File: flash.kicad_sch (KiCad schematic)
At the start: 0 parts

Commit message: [#103224] Add QSPI Flash section, add .ci.yml
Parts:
- added C5001: C_100n_0402, antmicro-footprints:C_0402_1005Metric, symbol antmicroCapacitors0402:C_100n_0402
- added C5002: C_100n_0402, antmicro-footprints:C_0402_1005Metric, symbol Capacitors0402:C_100n_0402
- added J5001: PinHeader_1x2_P2.54mm_Drill1.02mm, antmicro-footprints:PinHeader_1x2_P2.54mm_Drill1.02mm, symbol GenericPinHeaders:PinHeader_1x2_P2.54mm_Drill1.02mm
- added J5002: Socket_SOP2-16_ACA-SPI-006-K01_Flash_CUSTOM, antmicro-footprints:Socket_SOP2-16_ACA-SPI-006-K01, symbol MechanicalParts:Socket_SOP2-16_ACA-SPI-006-K01_Flash_CUSTOM
- added J5003: PinHeader_2x4_P2.54mm_Drill1.02mm, antmicro-footprints:PinHeader_2x4_P2.54mm_Drill1.02mm, symbol Antmicro Symbols:PinHeader_2x4_P2.54mm_Drill1.02mm
- added R5001, R5002, R5003, R5004, R5005, R5006, R5008: R_10k_0402, antmicro-footprints:R_0402_1005Metric, symbol antmicroResistors0402:R_10k_0402
- added R5007: R_1k_0402, antmicro-footprints:R_0402_1005Metric, symbol Antmicro Symbols:R_1k_0402
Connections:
- new net: J5001.1, R5007.1
- new net: J5002.3 (~{RESET}), R5008.1
- new net +1V8: C5001.2, C5002.2, J5002.14 (VIO), J5002.2 (VCC), J5003.1, R5001.2, R5002.2, R5003.2, R5004.2, R5005.2, R5006.2, R5008.2
- new net EC_QSPI.IO0: J5002.15 (SI/IO0), J5003.6, R5003.1
- new net EC_QSPI.IO1: J5002.8 (SO/IO1), J5003.5, R5004.1
- new net EC_QSPI.IO2: J5002.9 (~{WP/IO2}), J5003.7, R5005.1
- new net EC_QSPI.IO3: J5002.1 (~{HOLD/IO3}), J5003.8, R5006.1
- new net EC_QSPI.SCK: J5002.16 (SCK), J5003.4, R5001.1
- new net EC_QSPI.~{CS0}: J5002.7 (~{CS}), J5003.3, R5002.1, R5007.2
- new net GND: C5001.1, C5002.1, J5001.2, J5002.10 (VSS), J5003.2
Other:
- note added: "BSS_STRAP"
- note added: "From Eval: GigaDevice GD25LR256EFIR"
- note added: "QSPI Flash"

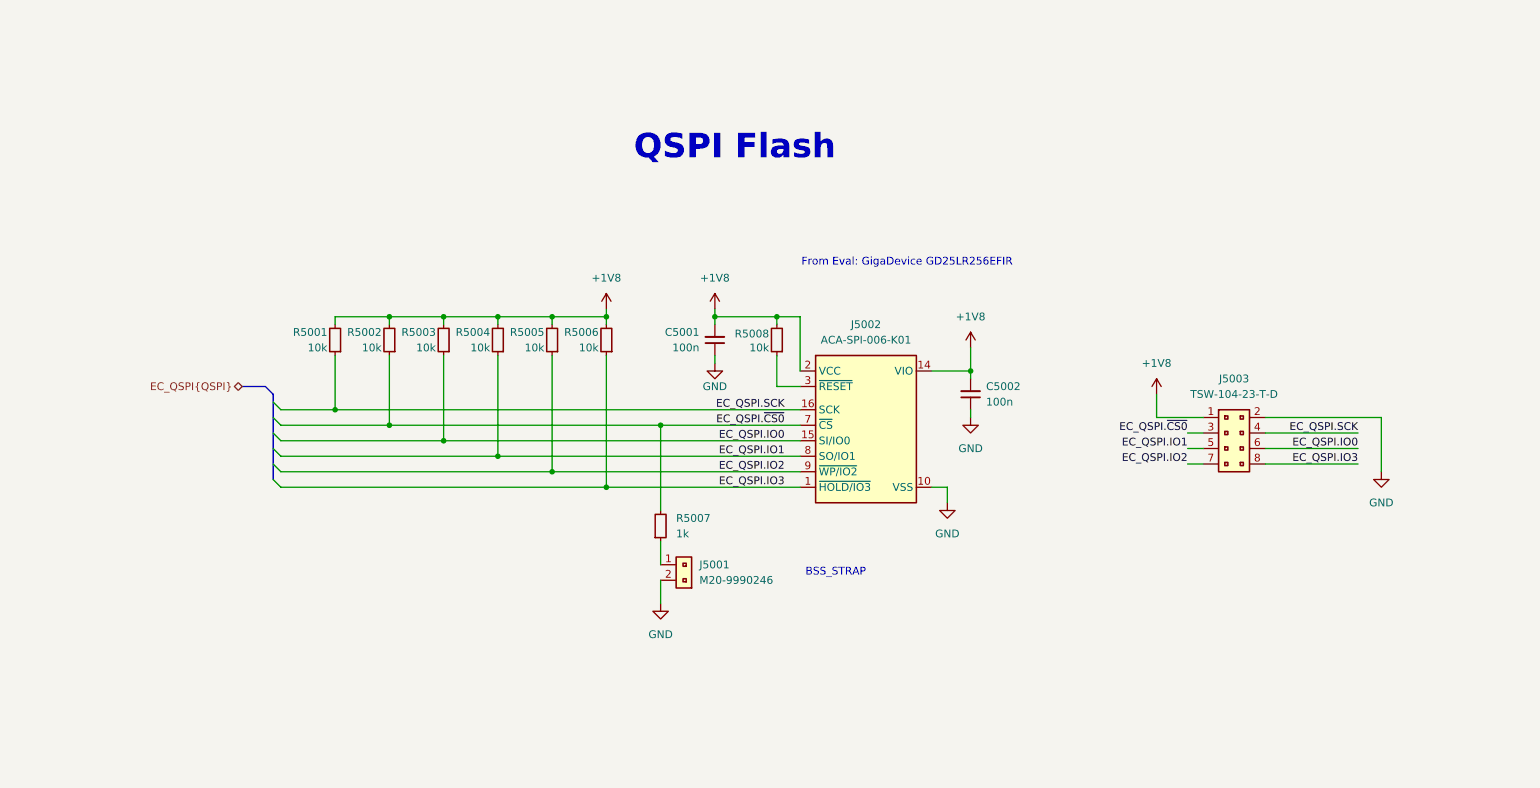
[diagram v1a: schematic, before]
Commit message: [#103224] Add JTAG connector, add 2nd QSPI flash in co-layout, add Antmicro and OSH logos
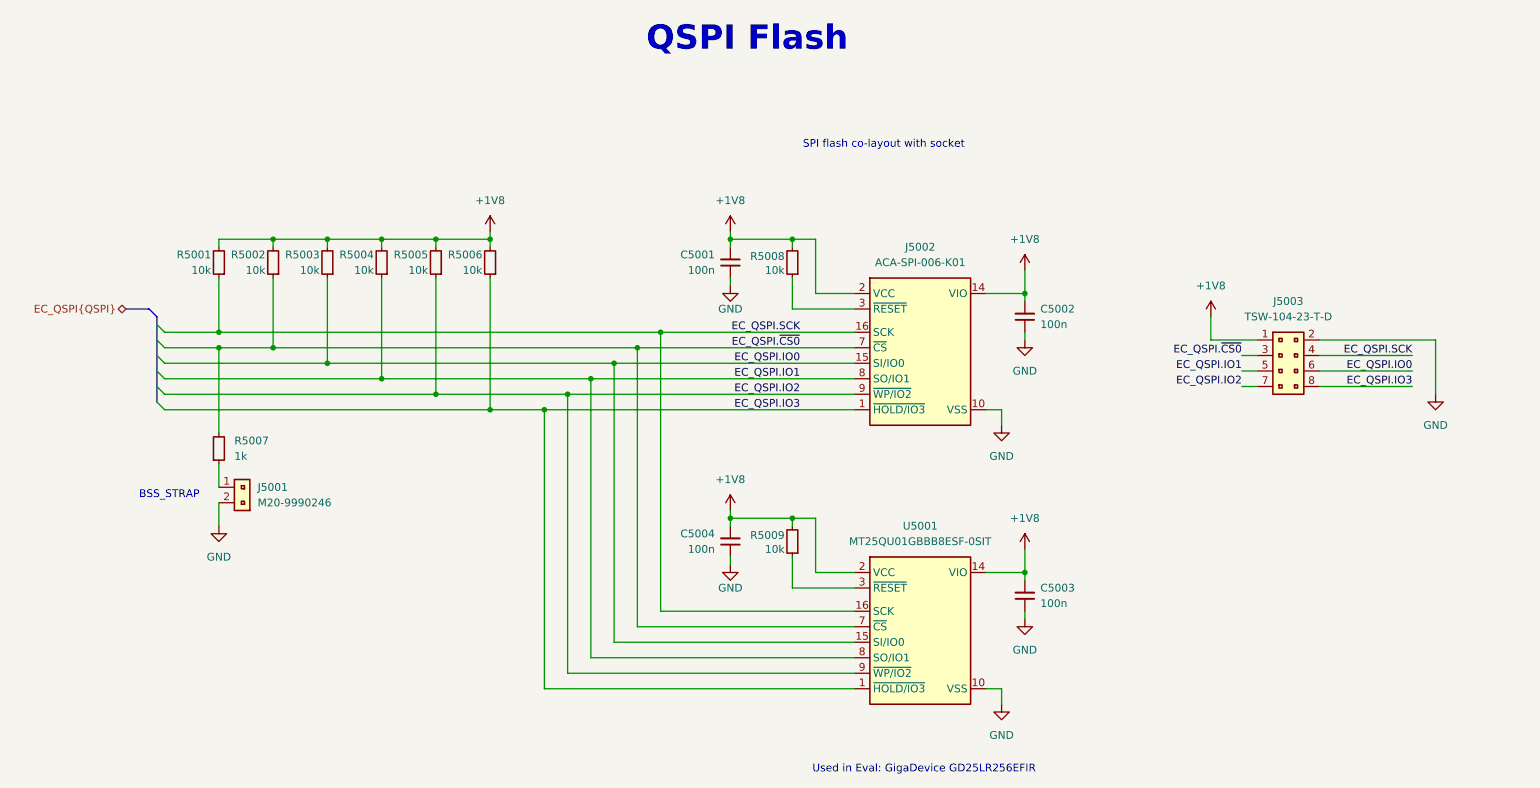
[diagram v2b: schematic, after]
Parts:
- added C5003: C_100n_0402, antmicro-footprints:C_0402_1005Metric, symbol Capacitors0402:C_100n_0402
- added C5004: C_100n_0402, antmicro-footprints:C_0402_1005Metric, symbol antmicroCapacitors0402:C_100n_0402
- added R5009: R_10k_0402, antmicro-footprints:R_0402_1005Metric, symbol antmicroResistors0402:R_10k_0402
- added U5001: MT25QU01GBBB8_SOIC, antmicro-footprints:SOIC-16_W7.5mm, symbol Antmicro Symbols:MT25QU01GBBB8_SOIC
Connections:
- net +1V8: now also C5003.2, C5004.2, R5009.2, U5001.14 (VIO), U5001.2 (VCC)
- net EC_QSPI.IO0: now also U5001.15 (SI/IO0)
- net EC_QSPI.IO1: now also U5001.8 (SO/IO1)
- net EC_QSPI.IO2: now also U5001.9 (~{WP/IO2})
- net EC_QSPI.IO3: now also U5001.1 (~{HOLD/IO3})
- net EC_QSPI.SCK: now also U5001.16 (SCK)
- net EC_QSPI.~{CS0}: now also U5001.7 (~{CS})
- net GND: now also C5003.1, C5004.1, U5001.10 (VSS)
- new net: U5001.11 (DNU), U5001.12 (DNU), U5001.4 (DNU), U5001.5 (DNU)
- new net: R5009.1, U5001.3 (~{RESET})
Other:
- note added: "SPI flash co-layout with socket"
- note added: "Used in Eval: GigaDevice GD25LR256EFIR"
- note removed: "From Eval: GigaDevice GD25LR256EFIR"
- moved on the sheet: C5001, C5002, J5001, J5002, J5003, R5001, R5002, R5003, R5004, R5005, R5006, R5007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

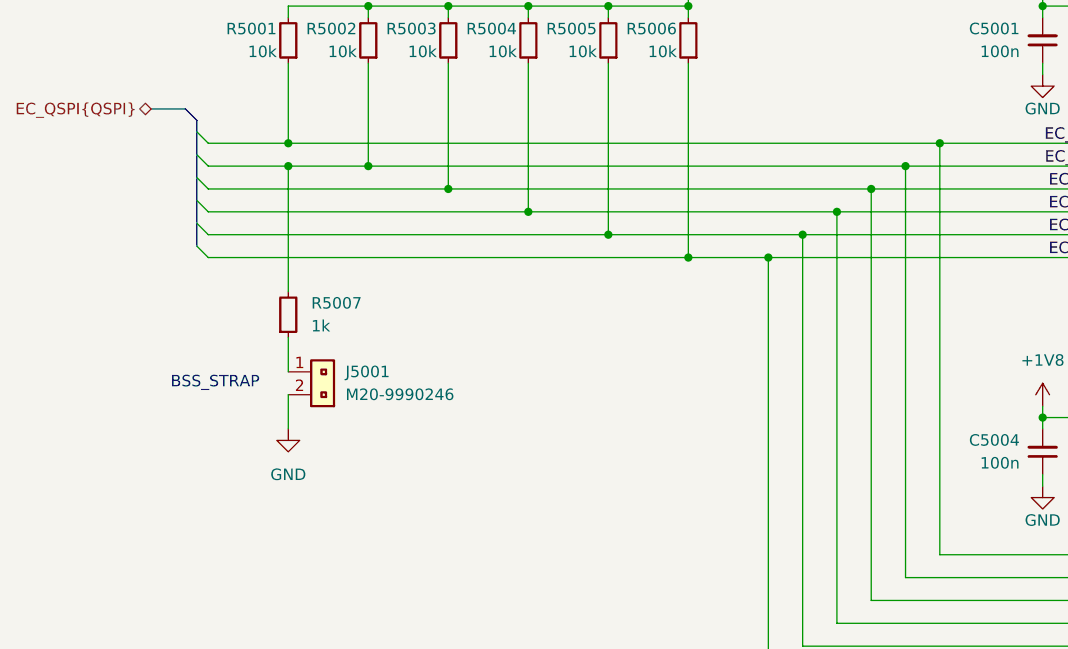
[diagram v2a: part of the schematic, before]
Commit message: [#103224] Change buffer ICs, change JTAG connector, move BSS_STRAP resistors to MEC1723 sheet
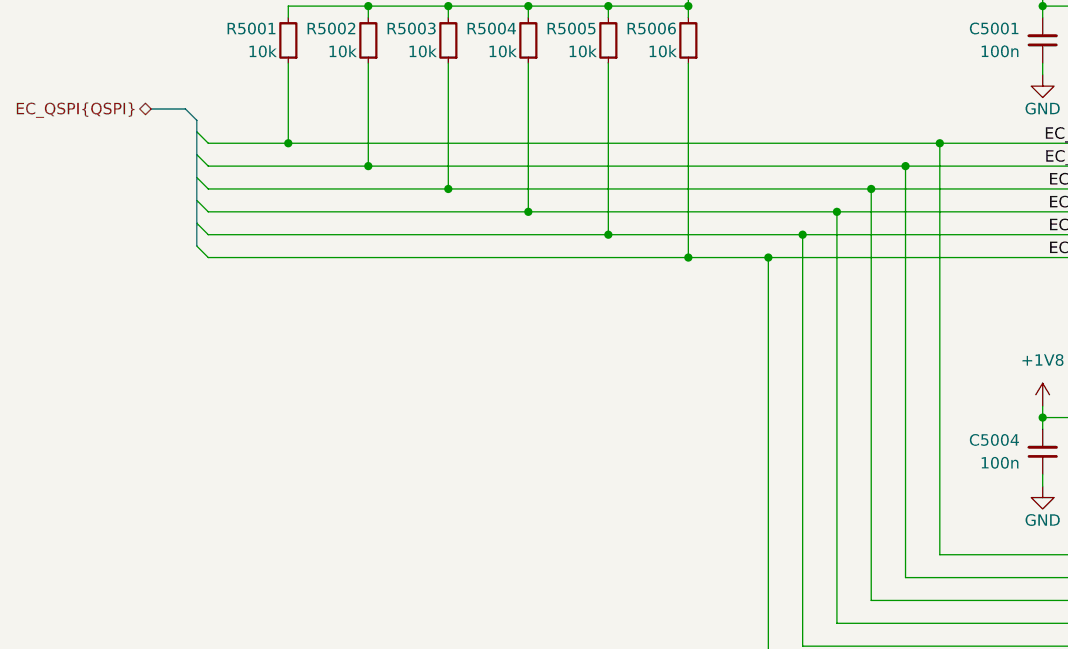
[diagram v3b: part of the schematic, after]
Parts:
- removed J5001: PinHeader_1x2_P2.54mm_Drill1.02mm, antmicro-footprints:PinHeader_1x2_P2.54mm_Drill1.02mm, symbol GenericPinHeaders:PinHeader_1x2_P2.54mm_Drill1.02mm
- removed R5007: R_1k_0402, antmicro-footprints:R_0402_1005Metric, symbol Antmicro Symbols:R_1k_0402
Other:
- note removed: "BSS_STRAP"

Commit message: [#103224] Route 7segment buffers, fix minor typos,add TODO list
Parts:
- added J5001: Tag-Connect_TC2050-IDC-NL_2x5_P1.27mm, antmicro-footprints:Tag-Connect_TC2050-IDC-NL_2x5_P1.27mm, symbol Antmicro Symbols:Tag-Connect_TC2050-IDC-NL_2x5_P1.27mm
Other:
- moved on the sheet: J5003
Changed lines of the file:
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@@
 	(wire
 		(pts
-			(xy 231.14 85.09) (xy 223.52 85.09)
+			(xy 238.76 67.31) (xy 231.14 67.31)
 		)
 		(stroke
@@
 	(wire
 		(pts
-			(xy 260.35 85.09) (xy 260.35 93.98)
+			(xy 267.97 67.31) (xy 267.97 76.2)
 		)
 		(stroke
@@
 	(wire
 		(pts
-			(xy 228.6 87.63) (xy 231.14 87.63)
+			(xy 236.22 69.85) (xy 238.76 69.85)
 		)
 		(stroke
@@
 	(wire
 		(pts
-			(xy 223.52 85.09) (xy 223.52 81.28)
+			(xy 231.14 67.31) (xy 231.14 63.5)
 		)
 		(stroke
@@
 	(wire
 		(pts
-			(xy 256.54 87.63) (xy 241.3 87.63)
+			(xy 264.16 69.85) (xy 248.92 69.85)
 		)
 		(stroke
@@
 	(wire
 		(pts
-			(xy 241.3 85.09) (xy 260.35 85.09)
+			(xy 248.92 67.31) (xy 267.97 67.31)
 		)
 		(stroke
@@
 	(wire
 		(pts
-			(xy 256.54 92.71) (xy 241.3 92.71)
+			(xy 264.16 74.93) (xy 248.92 74.93)
 		)
 		(stroke
@@
 	(wire
 		(pts
-			(xy 256.54 90.17) (xy 241.3 90.17)
+			(xy 264.16 72.39) (xy 248.92 72.39)
 		)
 		(stroke
@@
 	(wire
 		(pts
-			(xy 228.6 90.17) (xy 231.14 90.17)
+			(xy 236.22 72.39) (xy 238.76 72.39)
 		)
 		(stroke
@@
 	(wire
 		(pts
-			(xy 228.6 92.71) (xy 231.14 92.71)
+			(xy 236.22 74.93) (xy 238.76 74.93)
 		)
 		(stroke
@@
 	)
 	(label "EC_QSPI.IO0"
-		(at 256.54 90.17 180)
+		(at 264.16 72.39 180)
 		(effects
 			(font
@@
 	)
 	(label "EC_QSPI.~{CS0}"
-		(at 228.6 87.63 180)
+		(at 236.22 69.85 180)
 		(effects
 			(font
@@
 	)
 	(label "EC_QSPI.IO2"
-		(at 228.6 92.71 180)
+		(at 236.22 74.93 180)
 		(effects
 			(font
@@
 	)
 	(label "EC_QSPI.IO1"
-		(at 228.6 90.17 180)
+		(at 236.22 72.39 180)
 		(effects
 			(font
@@
 	)
 	(label "EC_QSPI.SCK"
-		(at 256.54 87.63 180)
+		(at 264.16 69.85 180)
 		(effects
 			(font
@@
 	)
 	(label "EC_QSPI.IO3"
-		(at 256.54 92.71 180)
+		(at 264.16 74.93 180)
 		(effects
 			(font
@@
 	(symbol
 		(lib_id "Antmicro Symbols:GND")
-		(at 260.35 93.98 0)
+		(at 267.97 76.2 0)
 		(unit 1)
 		(body_style 1)
@@
 		(fields_autoplaced yes)
 		(property "Reference" "#PWR05009"
-			(at 269.24 96.52 0)
+			(at 276.86 78.74 0)
 			(hide yes)
 			(show_name no)
@@
 		)
 		(property "Value" "GND"
-			(at 260.35 99.06 0)
+			(at 267.97 81.28 0)
 			(show_name no)
 			(do_not_autoplace no)
@@
 		)
 		(property "Footprint" ""
-			(at 269.24 101.6 0)
+			(at 276.86 83.82 0)
 			(hide yes)
 			(show_name no)
@@
 		)
 		(property "Datasheet" ""
-			(at 269.24 106.68 0)
+			(at 276.86 88.9 0)
 			(hide yes)
 			(show_name no)
@@
 		)
 		(property "Description" ""
-			(at 269.24 109.22 0)
+			(at 276.86 91.44 0)
 			(hide yes)
 			(show_name no)
@@
 		)
 		(property "Author" "Antmicro"
-			(at 269.24 101.6 0)
+			(at 276.86 83.82 0)
 			(hide yes)
 			(show_name no)
@@
 		)
 		(property "License" "Apache-2.0"
-			(at 269.24 104.14 0)
+			(at 276.86 86.36 0)
 			(hide yes)
 			(show_name no)
@@
 	(symbol
 		(lib_id "antmicropower:+1V8")
-		(at 223.52 81.28 0)
+		(at 231.14 63.5 0)
 		(unit 1)
 		(body_style 1)
@@
 		(fields_autoplaced yes)
 		(property "Reference" "#PWR05008"
-			(at 238.76 83.82 0)
+			(at 246.38 66.04 0)
 			(hide yes)
 			(show_name no)
@@
 		)
 		(property "Value" "+1V8"
-			(at 223.52 76.2 0)
+			(at 231.14 58.42 0)
 			(show_name no)
 			(do_not_autoplace no)
@@
 		)
 		(property "Footprint" ""
-			(at 238.76 88.9 0)
+			(at 246.38 71.12 0)
 			(hide yes)
 			(show_name no)
@@
 		)
 		(property "Datasheet" ""
-			(at 238.76 91.44 0)
+			(at 246.38 73.66 0)
 			(hide yes)
 			(show_name no)
@@
 		)
 		(property "Description" ""
-			(at 238.76 93.98 0)
+			(at 246.38 76.2 0)
 			(hide yes)
 			(show_name no)
@@
 		)
 		(property "Author" "Antmicro"
-			(at 238.76 86.36 0)
+			(at 246.38 68.58 0)
 			(hide yes)
 			(show_name no)
@@
 		)
 		(property "License" "Apache-2.0"
-			(at 238.76 88.9 0)
+			(at 246.38 71.12 0)
 			(hide yes)
 			(show_name no)
@@
 	(symbol
 		(lib_id "Antmicro Symbols:PinHeader_2x4_P2.54mm_Drill1.02mm")
-		(at 231.14 85.09 0)
+		(at 238.76 67.31 0)
 		(unit 1)
 		(body_style 1)
@@
 		(fields_autoplaced yes)
 		(property "Reference" "J5003"
-			(at 236.22 78.74 0)
+			(at 243.84 60.96 0)
 			(show_name no)
 			(do_not_autoplace no)
@@
 		)
 		(property "Value" "PinHeader_2x4_P2.54mm_Drill1.02mm"
-			(at 256.54 90.17 0)
+			(at 264.16 72.39 0)
 			(hide yes)
 			(show_name no)
@@
 		)
 		(property "Footprint" "antmicro-footprints:PinHeader_2x4_P2.54mm_Drill1.02mm"
-			(at 256.54 92.71 0)
+			(at 264.16 74.93 0)
 			(hide yes)
 			(show_name no)
@@
 		)
 		(property "Datasheet" "https://suddendocs.samtec.com/catalog_english/tsw_th.pdf"
-			(at 256.54 95.25 0)
+			(at 264.16 77.47 0)
 			(hide yes)
 			(show_name no)
@@
 		)
 		(property "Description" "Header 2.54mm pitch THT 8P in Dual Pin Header"
-			(at 256.54 107.95 0)
+			(at 264.16 90.17 0)
 			(hide yes)
 			(show_name no)
@@
 		)
 		(property "MPN" "TSW-104-23-T-D"
-			(at 236.22 81.28 0)
+			(at 243.84 63.5 0)
 			(show_name no)
 			(do_not_autoplace no)
@@
 		)
 		(property "Manufacturer" "Samtec"
-			(at 256.54 100.33 0)
+			(at 264.16 82.55 0)
 			(hide yes)
 			(show_name no)
@@
 		)
 		(property "Author" "Antmicro"
-			(at 256.54 102.87 0)
+			(at 264.16 85.09 0)
 			(hide yes)
 			(show_name no)
@@
 		)
 		(property "License" "Apache-2.0"
-			(at 256.54 105.41 0)
+			(at 264.16 87.63 0)
 			(hide yes)
 			(show_name no)
@@
 					(unit 1)
 				)
+			)
+		)
+	)
+	(symbol
+		(lib_id "Antmicro Symbols:Tag-Connect_TC2050-IDC-NL_2x5_P1.27mm")
+		(at 228.6 97.79 0)
+		(unit 1)
+		(body_style 1)
+		(exclude_from_sim no)
+		(in_bom no)
+		(on_board yes)
+		(in_pos_files yes)
+		(dnp no)
+		(fields_autoplaced yes)
+		(property "Reference" "J5001"
+			(at 244.475 90.17 0)
+			(show_name no)
+			(do_not_autoplace no)
+			(effects
+				(font
+					(size 1.27 1.27)
+					(thickness 0.15)
+				)
+			)
+		)
+		(property "Value" "Tag-Connect_TC2050-IDC-NL_2x5_P1.27mm"
+			(at 267.97 101.6 0)
+			(hide yes)
+			(show_name no)
+			(do_not_autoplace no)
+			(effects
+				(font
+					(size 1.27 1.27)
+					(thickness 0.15)
+				)
+				(justify left bottom)
+			)
+		)
+		(property "Footprint" "antmicro-footprints:Tag-Connect_TC2050-IDC-NL_2x5_P1.27mm"
+			(at 267.97 104.14 0)
+			(hide yes)
+			(show_name no)
+			(do_not_autoplace no)
+			(effects
+				(font
+					(size 1.27 1.27)
+					(thickness 0.15)
+				)
+				(justify left bottom)
+			)
+		)
+		(property "Datasheet" "https://www.tag-connect.com/wp-content/uploads/bsk-pdf-manager/TC2050-IDC-NL_Datasheet_8.pdf"
+			(at 267.97 106.68 0)
+			(hide yes)
+			(show_name no)
+			(do_not_autoplace no)
+			(effects
+				(font
+					(size 1.27 1.27)
+					(thickness 0.15)
+				)
+				(justify left bottom)
+			)
+		)
+		(property "Description" "Tag Connect 2x5 1.27mm terminal"
+			(at 267.97 119.38 0)
+			(hide yes)
+			(show_name no)
+			(do_not_autoplace no)
+			(effects
+				(font
+					(size 1.27 1.27)
+				)
+				(justify left bottom)
+			)
+		)
+		(property "MPN" "TC2050-IDC-NL"
+			(at 244.475 92.71 0)
+			(show_name no)
+			(do_not_autoplace no)
+			(effects
+				(font
+					(size 1.27 1.27)
+					(thickness 0.15)
+				)
+			)
+		)
+		(property "Manufacturer" "Tag Connect"
+			(at 267.97 111.76 0)
+			(hide yes)
+			(show_name no)
+			(do_not_autoplace no)
+			(effects
+				(font
+					(size 1.27 1.27)
+					(thickness 0.15)
+				)
+				(justify left bottom)
+			)
+		)
+		(property "Author" "Antmicro"
+			(at 267.97 114.3 0)
+			(hide yes)
+			(show_name no)
+			(do_not_autoplace no)
+			(effects
+				(font
+					(size 1.27 1.27)
+					(thickness 0.15)
+				)
+				(justify left bottom)
+			)
+		)
+		(property "License" "Apache-2.0"
+			(at 267.97 116.84 0)
+			(hide yes)
+			(show_name no)
+			(do_not_autoplace no)
+			(effects
+				(font
+					(size 1.27 1.27)
+					(thickness 0.15)
+				)
+				(justify left bottom)
+			)
+		)
+		(pin "2"
+		)
+		(pin "6"
+		)
+		(pin "8"
+		)
+		(pin "3"
+		)
+		(pin "7"
+		)
+		(pin "4"
+		)
+		(pin "10"
+		)
+		(pin "5"
+		)
+		(pin "9"
+		)
+		(pin "1"
+		)
+		(instances
+			(project "dc-scm-server-integration-espi-adapter"
+				(path "/df391740-647e-4ab6-9dcd-d61184d66fe9/870b0b62-f962-4a87-8d30-5a8522c5db60"
+					(reference "J5001")
+					(unit 1)
+				)
